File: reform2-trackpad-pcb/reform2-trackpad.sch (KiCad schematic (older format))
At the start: 22 parts, among them J1 Conn_USB, J2 Conn_01x06_Female, SW6 SW_RST, SW7 SW_HWB, U1 ATmega32U2-AU, U2 TLV75533PDBV, Y1 Crystal_GND24

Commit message: reform2-trackpad: components cleanup
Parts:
- SW7: Manufacturer Omron -> Apem; Manufacturer_No A6S-1101-H -> DM01
- U2: symbol Regulator_Linear:TLV75533PDBV -> reform2-trackpad-rescue:TLV75533PDBV-Regulator_Linear
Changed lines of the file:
@@
 F 1 "ATmega32U2-AU" H 5000 2000 50  0000 C CNN
 F 2 "Package_QFP:TQFP-32_7x7mm_P0.8mm" H 4600 3450 50  0001 C CIN
-F 3 "http://ww1.microchip.com/downloads/en/DeviceDoc/doc7799.pdf" H 4600 3450 50  0001 C CNN
+F 3 "" H 4600 3450 50  0001 C CNN
 F 4 "Microchip" H 4600 3450 50  0001 C CNN "Manufacturer"
 F 5 "ATMEGA32U2-AU" H 4600 3450 50  0001 C CNN "Manufacturer_No"
@@
 F 1 "Conn_USB" H 1450 2950 50  0000 C CNN
 F 2 "Connector_JST:JST_PH_B4B-PH-K_1x04_P2.00mm_Vertical" H 1700 3050 50  0001 C CNN
-F 3 "~" H 1700 3050 50  0001 C CNN
+F 3 "" H 1700 3050 50  0001 C CNN
 F 4 "JST" H 1700 3050 50  0001 C CNN "Manufacturer"
 F 5 "B4B-PH-K-S(LF)(SN)" H 1700 3050 50  0001 C CNN "Manufacturer_No"
@@
 F 1 "0.1uF" H 3042 2005 50  0000 L CNN
 F 2 "Capacitor_SMD:C_0603_1608Metric" H 2950 2050 50  0001 C CNN
-F 3 "~" H 2950 2050 50  0001 C CNN
+F 3 "" H 2950 2050 50  0001 C CNN
 F 4 "Yageo" H 2950 2050 50  0001 C CNN "Manufacturer"
 F 5 "CC0603JPX7R9BB104" H 2950 2050 50  0001 C CNN "Manufacturer_No"
@@
 F 1 "1uF" H 3642 3355 50  0000 L CNN
 F 2 "Capacitor_SMD:C_0603_1608Metric" H 3550 3400 50  0001 C CNN
-F 3 "~" H 3550 3400 50  0001 C CNN
+F 3 "" H 3550 3400 50  0001 C CNN
 F 4 "Taiyo Yuden" H 3550 3400 50  0001 C CNN "Manufacturer"
 F 5 "UMK107BJ105KA-T" H 3550 3400 50  0001 C CNN "Manufacturer_No"
@@
 F 1 "10k" H 6559 4155 50  0000 L CNN
 F 2 "Resistor_SMD:R_0603_1608Metric" H 6500 4200 50  0001 C CNN
-F 3 "~" H 6500 4200 50  0001 C CNN
+F 3 "" H 6500 4200 50  0001 C CNN
 F 4 "Vishay Dale" H 6500 4200 50  0001 C CNN "Manufacturer"
 F 5 "CRCW060310K0JNEAC" H 6500 4200 50  0001 C CNN "Manufacturer_No"
@@
 F 1 "10k" H 3859 2005 50  0000 L CNN
 F 2 "Resistor_SMD:R_0603_1608Metric" H 3800 2050 50  0001 C CNN
-F 3 "~" H 3800 2050 50  0001 C CNN
+F 3 "" H 3800 2050 50  0001 C CNN
 F 4 "Vishay Dale" H 3800 2050 50  0001 C CNN "Manufacturer"
 F 5 "CRCW060310K0JNEAC" H 3800 2050 50  0001 C CNN "Manufacturer_No"
@@
 F 1 "18pF" V 2512 2550 50  0000 C CNN
 F 2 "Capacitor_SMD:C_0603_1608Metric" H 2650 2550 50  0001 C CNN
-F 3 "~" H 2650 2550 50  0001 C CNN
+F 3 "" H 2650 2550 50  0001 C CNN
 F 4 "Yageo" H 2650 2550 50  0001 C CNN "Manufacturer"
 F 5 "CC0603JRNPO9BN180" H 2650 2550 50  0001 C CNN "Manufacturer_No"
@@
 F 1 "18pF" V 2500 2750 50  0000 C CNN
 F 2 "Capacitor_SMD:C_0603_1608Metric" H 2650 2750 50  0001 C CNN
-F 3 "~" H 2650 2750 50  0001 C CNN
+F 3 "" H 2650 2750 50  0001 C CNN
 F 4 "Yageo" H 2650 2750 50  0001 C CNN "Manufacturer"
 F 5 "CC0603JRNPO9BN180" H 2650 2750 50  0001 C CNN "Manufacturer_No"
@@
 F 1 "Crystal_GND24" V 3095 2891 50  0000 L CNN
 F 2 "Crystal:Crystal_SMD_3225-4Pin_3.2x2.5mm_HandSoldering" H 3050 2650 50  0001 C CNN
-F 3 "~" H 3050 2650 50  0001 C CNN
+F 3 "" H 3050 2650 50  0001 C CNN
 F 4 "Abracon" H 3050 2650 50  0001 C CNN "Manufacturer"
 F 5 "ABM8AIG-16.000MHz-4-T" H 3050 2650 50  0001 C CNN "Manufacturer_No"
@@
 F 1 "Conn_01x06_Female" V 6850 2900 50  0000 R CNN
 F 2 "Connector_FFC-FPC:Hirose_FH12-6S-0.5SH_1x06-1MP_P0.50mm_Horizontal" H 6750 2500 50  0001 C CNN
-F 3 "~" H 6750 2500 50  0001 C CNN
+F 3 "" H 6750 2500 50  0001 C CNN
 F 4 "Hirose" H 6750 2500 50  0001 C CNN "Manufacturer"
 F 5 "FH12-6S-0.5SH(55)" H 6750 2500 50  0001 C CNN "Manufacturer_No"
@@
 F 1 "SW_HWB" V 6845 4380 50  0000 L CNN
 F 2 "Button_Switch_SMD:SW_DIP_SPSTx01_Slide_Omron_A6S-110x_W8.9mm_P2.54mm" H 6800 4250 50  0001 C CNN
-F 3 "~" H 6800 4250 50  0001 C CNN
-F 4 "Omron" H 6800 4250 50  0001 C CNN "Manufacturer"
-F 5 "A6S-1101-H" H 6800 4250 50  0001 C CNN "Manufacturer_No"
+F 3 "" H 6800 4250 50  0001 C CNN
+F 4 "Apem" H 6800 4250 50  0001 C CNN "Manufacturer"
+F 5 "DM01" H 6800 4250 50  0001 C CNN "Manufacturer_No"
 	1    6800 4250
 	0    1    1    0
@@
 F 1 "SW_RST" H 3500 1744 50  0000 C CNN
 F 2 "Button_Switch_SMD:SW_Push_1P1T_NO_CK_KMR2" H 3500 1750 50  0001 C CNN
-F 3 "~" H 3500 1750 50  0001 C CNN
+F 3 "" H 3500 1750 50  0001 C CNN
 F 4 "CK" H 3500 1550 50  0001 C CNN "Manufacturer"
 F 5 "KMR221GLFS" H 3500 1550 50  0001 C CNN "Manufacturer_No"
@@
 	3700 2350 3700 1550
 $Comp
-L Regulator_Linear:TLV75533PDBV U2
+L reform2-trackpad-rescue:TLV75533PDBV-Regulator_Linear U2
 U 1 1 5DAEEA1F
 P 8550 2000
@@
 F 1 "TLV75533PDBV" H 8550 2251 50  0000 C CNN
 F 2 "Package_TO_SOT_SMD:SOT-23-5" H 8550 2300 50  0001 C CIN
-F 3 "http://www.ti.com/lit/ds/symlink/tlv755p.pdf" H 8550 2000 50  0001 C CNN
+F 3 "" H 8550 2000 50  0001 C CNN
 F 4 "Texas Instruments" H 8550 2000 50  0001 C CNN "Manufacturer"
 F 5 "TLV75533PDBVR" H 8550 2000 50  0001 C CNN "Manufacturer_No"
@@
 F 1 "0.1uF" H 8092 2205 50  0000 L CNN
 F 2 "Capacitor_SMD:C_0603_1608Metric" H 8000 2250 50  0001 C CNN
-F 3 "~" H 8000 2250 50  0001 C CNN
+F 3 "" H 8000 2250 50  0001 C CNN
 F 4 "Yageo" H 8000 2250 50  0001 C CNN "Manufacturer"
 F 5 "CC0603JPX7R9BB104" H 8000 2250 50  0001 C CNN "Manufacturer_No"
+F 6 "" H 8000 2250 50  0001 C CNN "DNP"
+F 7 "" H 8000 2250 50  0001 C CNN "Flags"
 	1    8000 2250
 	1    0    0    -1
@@
 F 1 "22" V 2250 2950 50  0000 C CNN
 F 2 "Resistor_SMD:R_0603_1608Metric" H 2250 2950 50  0001 C CNN
-F 3 "~" H 2250 2950 50  0001 C CNN
+F 3 "" H 2250 2950 50  0001 C CNN
 F 4 "Yageo" H 2250 2950 50  0001 C CNN "Manufacturer"
 F 5 "RT0603DRD0722RL" H 2250 2950 50  0001 C CNN "Manufacturer_No"
@@
 F 1 "22" V 2250 3050 50  0000 C CNN
 F 2 "Resistor_SMD:R_0603_1608Metric" H 2250 3050 50  0001 C CNN
-F 3 "~" H 2250 3050 50  0001 C CNN
+F 3 "" H 2250 3050 50  0001 C CNN
 F 4 "Yageo" H 2250 3050 50  0001 C CNN "Manufacturer"
 F 5 "RT0603DRD0722RL" H 2250 3050 50  0001 C CNN "Manufacturer_No"
@@
 F 1 "4.7k" V 6450 1150 50  0000 C CNN
 F 2 "Resistor_SMD:R_0603_1608Metric" H 6450 1150 50  0001 C CNN
-F 3 "~" H 6450 1150 50  0001 C CNN
+F 3 "" H 6450 1150 50  0001 C CNN
 F 4 "Yageo" H 6450 1150 50  0001 C CNN "Manufacturer"
 F 5 "RC0603FR-074K7L" H 6450 1150 50  0001 C CNN "Manufacturer_No"
@@
 F 1 "4.7k" V 6700 1250 50  0000 C CNN
 F 2 "Resistor_SMD:R_0603_1608Metric" H 6700 1250 50  0001 C CNN
-F 3 "~" H 6700 1250 50  0001 C CNN
+F 3 "" H 6700 1250 50  0001 C CNN
 F 4 "Yageo" H 6700 1250 50  0001 C CNN "Manufacturer"
 F 5 "RC0603FR-074K7L" H 6700 1250 50  0001 C CNN "Manufacturer_No"

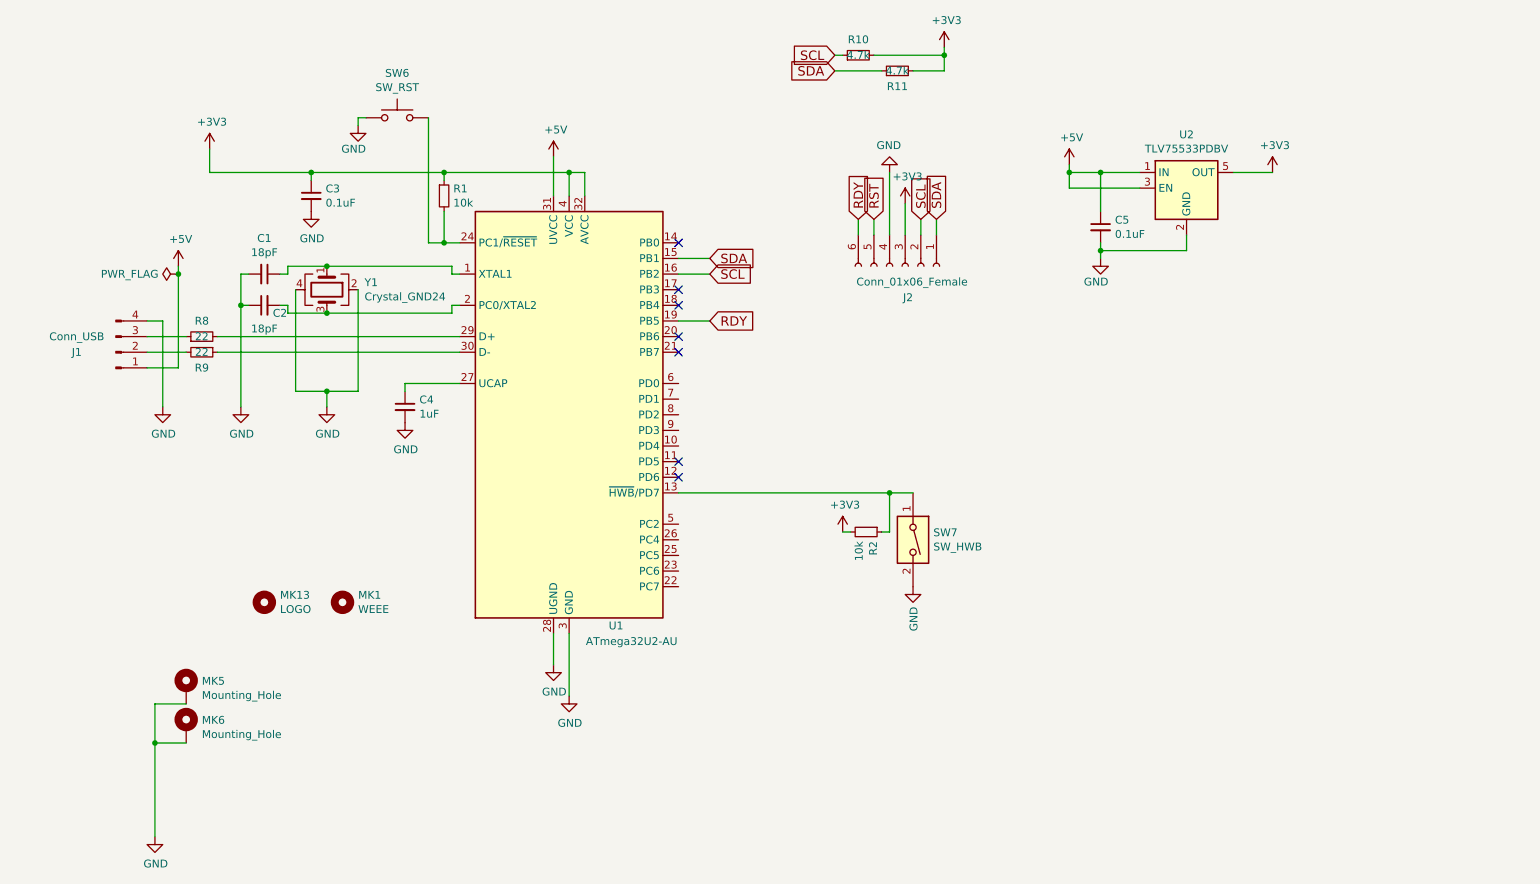
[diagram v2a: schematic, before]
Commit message: trackpad: add ESD protection and fuse, add badge, bump to R-1
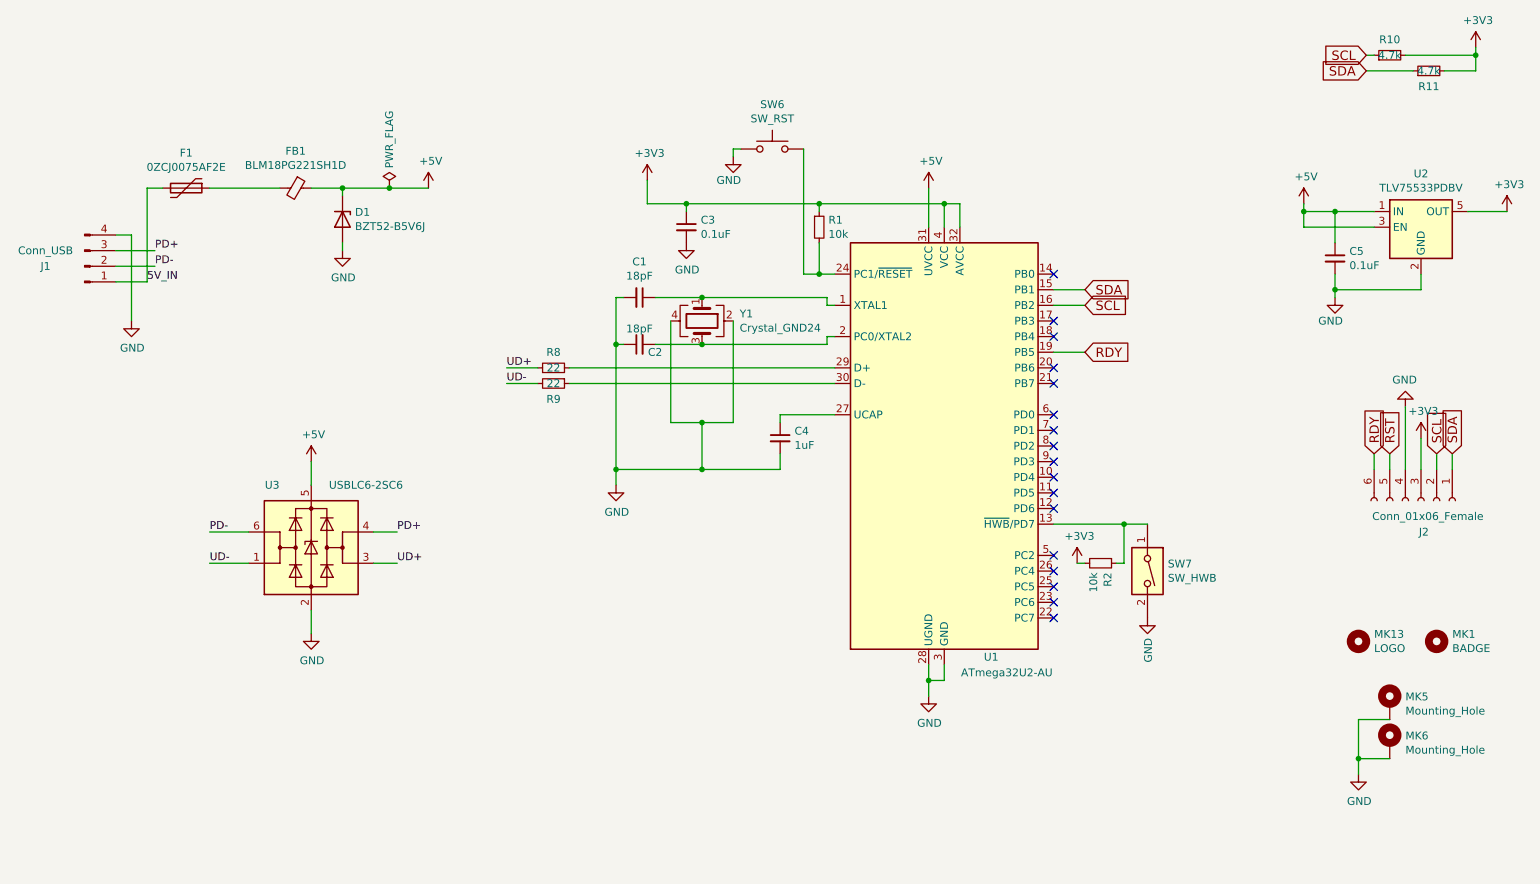
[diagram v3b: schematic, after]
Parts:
- added D1: BZT52-B5V6J, Diode_SMD:D_SOD-123, symbol Device:D_Zener
- added F1: 0ZCJ0075AF2E, Fuse:Fuse_1206_3216Metric_Castellated, symbol Device:Polyfuse
- added FB1: BLM18PG221SH1D, Inductor_SMD:L_0603_1608Metric, symbol Device:Ferrite_Bead_Small
- added U3: USBLC6-2SC6, Package_TO_SOT_SMD:SOT-23-6, symbol Power_Protection:USBLC6-2SC6
- MK1: value WEEE -> BADGE; footprint Symbol:WEEE-Logo_4.2x6mm_SilkScreen -> footprints:reform2-trackpadctrl-badge; DNP (none) -> y
- MK13, MK5, MK6: DNP (none) -> y
- Y1: footprint Crystal:Crystal_SMD_3225-4Pin_3.2x2.5mm_HandSoldering -> Crystal:Crystal_SMD_3225-4Pin_3.2x2.5mm
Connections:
- net +5V: now also D1.1 (K), FB1.1, U3.5 (VBUS); no longer J1.1 (Pin_1)
- net GND: now also D1.2 (A), U3.2 (GND)
- net PD-: now reaches J1.2 (Pin_2)
- net PD-: now also U3.6 (I/O1); no longer R9.2
- net PD+: now reaches J1.3 (Pin_3)
- net PD+: now also U3.4 (I/O2); no longer R8.1
- new net: F1.1, FB1.2
- new net 5V_IN: F1.2, J1.1 (Pin_1)
- new net UD+: R8.1, U3.3 (I/O2)
- new net UD-: R9.2, U3.1 (I/O1)
- no-connect marks 7 -> 17
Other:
- moved on the sheet: C1, C2, C3, C4, C5, J1, J2, MK1, MK13, MK5, MK6, R1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
